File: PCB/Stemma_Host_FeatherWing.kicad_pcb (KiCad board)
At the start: 2 copper layers, 50.8 x 22.9 mm, 17 parts, among them J1 STEMMA, J2 STEMMA, J3 STEMMA-QT, J4 STEMMA-QT, M1 Feather_M4_Express, U1 BSS138DW-Y-F_ALT, U2 AP2112-3.3

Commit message: update with initial design
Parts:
- removed C2: 0.1uF, Capacitors_SMD:C_0805
- removed C3: 10uF, Capacitors_SMD:C_0805
- removed U2: AP2112-3.3, TO_SOT_Packages_SMD:SOT-23-5
- added D2: MBR120, Diodes_SMD:D_SOD-123F, F.Cu at (122.1, 99.8)
- added D3: MBR120, Diodes_SMD:D_SOD-123F, F.Cu at (125.7, 99.8)
- added SW1: RESET, Adafruit:TL3330AF_SPST_BUTTON_RT-ANGLE_7.8mm_2.5mm_2.5mm, F.Cu at (117.3, 85.5)
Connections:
- M1 pad 1: (no net) -> /~RST
- M1 pad 17: (no net) -> /BAT
- M1 pad 19: (no net) -> /USB
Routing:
- net /USB: track 0.00 -> 31.2 mm, vias 0 -> 1
- net /~RST: track 0.00 -> 24.0 mm, vias 0 -> 1
- net /BAT: track 0.00 -> 22.7 mm, vias 0 -> 1
- net /+V: track 84.3 -> 72.1 mm, vias 4 -> 3
- net +3V3: track 39.4 -> 35.4 mm
- net GND: vias 13 -> 14
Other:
- board text added: "2019-11-26 v01"
- board text added: "A Feather-powered Stemma FeatherWing. The host Feather provides 3.3V or ~5V for the Stemma connector."
- board text added: "Stemma Host FeatherWing"
- board text removed: "2019-11-26 v02"
- board text removed: "A Stemma-powered interface backpack for FeatherWings. The Stemma connector provides +3.3V to the attached Wing."
- board text removed: "StemmaWing Backpack"

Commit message: update design
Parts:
- added JMP3: STEMMA_TYPE, Connectors:GS3, B.Cu at (141.7, 109.5)
- SW1: value RESET -> SW_Push
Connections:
- J1 pad 3: /+V -> Net-(J1-Pad3)
- J2 pad 3: /+V -> Net-(J1-Pad3)
- J3 pad 3: /+V -> Net-(J1-Pad3)
- J4 pad 3: /+V -> Net-(J1-Pad3)
- RN1 pad 1: /+V -> Net-(J1-Pad3)
- RN1 pad 4: /+V -> Net-(J1-Pad3)
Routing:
- net /+V: track 72.1 -> 74.1 mm
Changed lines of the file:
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@@
     (thickness 1.6)
     (drawings 3434)
-    (tracks 255)
+    (tracks 257)
     (zones 0)
-    (modules 17)
-    (nets 14)
+    (modules 18)
+    (nets 15)
   )
   (page USLetter)
@@
     (35 F.Paste user hide)
     (36 B.SilkS user)
-    (37 F.SilkS user)
+    (37 F.SilkS user hide)
     (38 B.Mask user)
-    (39 F.Mask user)
+    (39 F.Mask user hide)
     (40 Dwgs.User user hide)
     (41 Cmts.User user hide)
@@
   (net 12 /USB)
   (net 13 /~RST)
+  (net 14 "Net-(J1-Pad3)")
   (net_class Default "This is the default net class."
     (clearance 0.1524)
@@
     (add_net /~RST)
     (add_net "Net-(D1-Pad2)")
+    (add_net "Net-(J1-Pad3)")
   )
   (net_class Power ""
@@
       (net 1 GND))
     (pad 3 smd rect (at 0.5 -1.9375 270) (size 0.6 1.55) (layers F.Cu F.Paste F.Mask)
-      (net 7 /+V))
+      (net 14 "Net-(J1-Pad3)"))
     (pad 2 smd rect (at -0.5 -1.9375 270) (size 0.6 1.55) (layers F.Cu F.Paste F.Mask)
       (net 6 /STEMMA_SDA))
@@
       (net 1 GND))
     (pad 3 smd rect (at 0.5 -1.9375 90) (size 0.6 1.55) (layers F.Cu F.Paste F.Mask)
-      (net 7 /+V))
+      (net 14 "Net-(J1-Pad3)"))
     (pad 2 smd rect (at -0.5 -1.9375 90) (size 0.6 1.55) (layers F.Cu F.Paste F.Mask)
       (net 6 /STEMMA_SDA))
@@
       (net 3 /SDA))
     (pad 4 smd rect (at -0.9 1.2) (size 0.8 0.5) (layers F.Cu F.Paste F.Mask)
-      (net 7 /+V))
+      (net 14 "Net-(J1-Pad3)"))
     (pad 2 smd rect (at -0.9 -0.4) (size 0.8 0.4) (layers F.Cu F.Paste F.Mask)
       (net 4 +3V3))
@@
       (net 4 +3V3))
     (pad 1 smd rect (at -0.9 -1.2) (size 0.8 0.5) (layers F.Cu F.Paste F.Mask)
-      (net 7 /+V))
+      (net 14 "Net-(J1-Pad3)"))
     (model ${KISYS3DMOD}/Resistors_SMD.3dshapes/R_Array_Convex_4x0603.wrl
       (at (xyz 0 0 0))
@@
       (net 6 /STEMMA_SDA))
     (pad 3 smd rect (at 1 -2.875 270) (size 1 3.5) (layers F.Cu F.Paste F.Mask)
-      (net 7 /+V))
+      (net 14 "Net-(J1-Pad3)"))
     (pad 4 smd rect (at 3 -2.875 270) (size 1 3.5) (layers F.Cu F.Paste F.Mask)
       (net 1 GND))
@@
       (net 1 GND))
     (pad 3 smd rect (at 1 -2.875 90) (size 1 3.5) (layers F.Cu F.Paste F.Mask)
-      (net 7 /+V))
+      (net 14 "Net-(J1-Pad3)"))
     (pad 2 smd rect (at -1 -2.875 90) (size 1 3.5) (layers F.Cu F.Paste F.Mask)
       (net 6 /STEMMA_SDA))
@@
       (effects (font (size 0.5 0.5) (thickness 0.1)))
     )
-    (fp_text value RESET (at 0 2.1) (layer F.SilkS)
+    (fp_text value SW_Push (at 0 2.1) (layer F.SilkS)
       (effects (font (size 0.6 0.6) (thickness 0.12)))
     )
@@
     )
   )
+  (module Connectors:GS3 (layer B.Cu)
+    (at 141.7 109.5)
+    (descr "3-pin solder bridge")
+    (tags "solder bridge")
+    (attr smd)
+    (fp_text reference JMP3 (at -1.7 0 -90) (layer B.SilkS)
+      (effects (font (size 1 1) (thickness 0.15)) (justify mirror))
+    )
+    (fp_text value STEMMA_TYPE (at 1.8 0 -90) (layer B.Fab)
+      (effects (font (size 1 1) (thickness 0.15)) (justify mirror))
+    )
+    (fp_line (start -1.15 2.15) (end 1.15 2.15) (layer B.CrtYd) (width 0.05))
+    (fp_line (start 1.15 2.15) (end 1.15 -2.15) (layer B.CrtYd) (width 0.05))
+    (fp_line (start 1.15 -2.15) (end -1.15 -2.15) (layer B.CrtYd) (width 0.05))
+    (fp_line (start -1.15 -2.15) (end -1.15 2.15) (layer B.CrtYd) (width 0.05))
+    (fp_line (start -0.89 1.91) (end -0.89 -1.91) (layer B.SilkS) (width 0.12))
+    (fp_line (start -0.89 -1.91) (end 0.89 -1.91) (layer B.SilkS) (width 0.12))
+    (fp_line (start 0.89 -1.91) (end 0.89 1.91) (layer B.SilkS) (width 0.12))
+    (fp_line (start -0.89 1.91) (end 0.89 1.91) (layer B.SilkS) (width 0.12))
+    (pad 1 smd rect (at 0 1.27) (size 1.27 0.97) (layers B.Cu B.Paste B.Mask)
+      (net 4 +3V3))
+    (pad 2 smd rect (at 0 0) (size 1.27 0.97) (layers B.Cu B.Paste B.Mask)
+      (net 14 "Net-(J1-Pad3)"))
+    (pad 3 smd rect (at 0 -1.27) (size 1.27 0.97) (layers B.Cu B.Paste B.Mask)
+      (net 7 /+V))
+  )
   (gr_line (start 144.970789 88.408715) (end 144.970789 88.387715) (layer F.SilkS) (width 0.1))
   (gr_line (start 145.055489 88.324715) (end 145.055489 88.302715) (layer F.SilkS) (width 0.1))
@@
   (segment (start 129.421937 101.2) (end 129.880683 101.658746) (width 0.1524) (layer F.Cu) (net 7))
   (segment (start 125.7 101.2) (end 129.421937 101.2) (width 0.1524) (layer F.Cu) (net 7))
+  (segment (start 155.829 94.75) (end 155.829 93.129) (width 0.1524) (layer B.Cu) (net 7))
+  (segment (start 155.829 93.129) (end 155.5 92.8) (width 0.1524) (layer B.Cu) (net 7))
   (segment (start 132.969 99.908746) (end 132.969 99.406346) (width 0.1524) (layer F.Cu) (net 8))
   (segment (start 132.969 99.406346) (end 132.969 98.171) (width 0.1524) (layer F.Cu) (net 8))

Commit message: initial repo load
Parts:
- SW1: value SW_Push -> RESET
- U1: value BSS138DW-Y-F_ALT -> BSS138DW-Y-F
- moved JMP3 33.5 mm to (113.9, 90.8)
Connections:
- J1 pad 3: Net-(J1-Pad3) -> /+V
- J2 pad 3: Net-(J1-Pad3) -> /+V
- J3 pad 3: Net-(J1-Pad3) -> /+V
- J4 pad 3: Net-(J1-Pad3) -> /+V
- JMP3 pad 2: Net-(J1-Pad3) -> /+V
- RN1 pad 1: Net-(J1-Pad3) -> /+V
- RN1 pad 4: Net-(J1-Pad3) -> /+V
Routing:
- net /+V: track 74.1 -> 120.9 mm, vias 3 -> 4
- net +3V3: track 35.4 -> 52.5 mm, vias 0 -> 1
- net /STEMMA_SDA: track 48.0 -> 53.6 mm
- net /STEMMA_SCL: track 51.6 -> 49.5 mm
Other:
- board text added: "2019-11-27 v01"
- board text added: "3V"
- board text added: "A Feather-powered Stemma FeatherWing. The host Feather provides 3.3V or ~~5V for the Stemma connector."
- board text added: "Stemma +V"
- board text added: "~~5V"
- board text removed: "2019-11-26 v01"
- board text removed: "A Feather-powered Stemma FeatherWing. The host Feather provides 3.3V or ~5V for the Stemma connector."

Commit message: PCB version update
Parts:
- U1: value BSS138DW-Y-F -> BSS138; footprint TO_SOT_Packages_SMD:SOT-23-6 -> TO_SOT_Packages_SMD:SOT-363_SC-70-6
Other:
- board text added: "2019-12-09 v02"
- board text removed: "2019-11-27 v01"

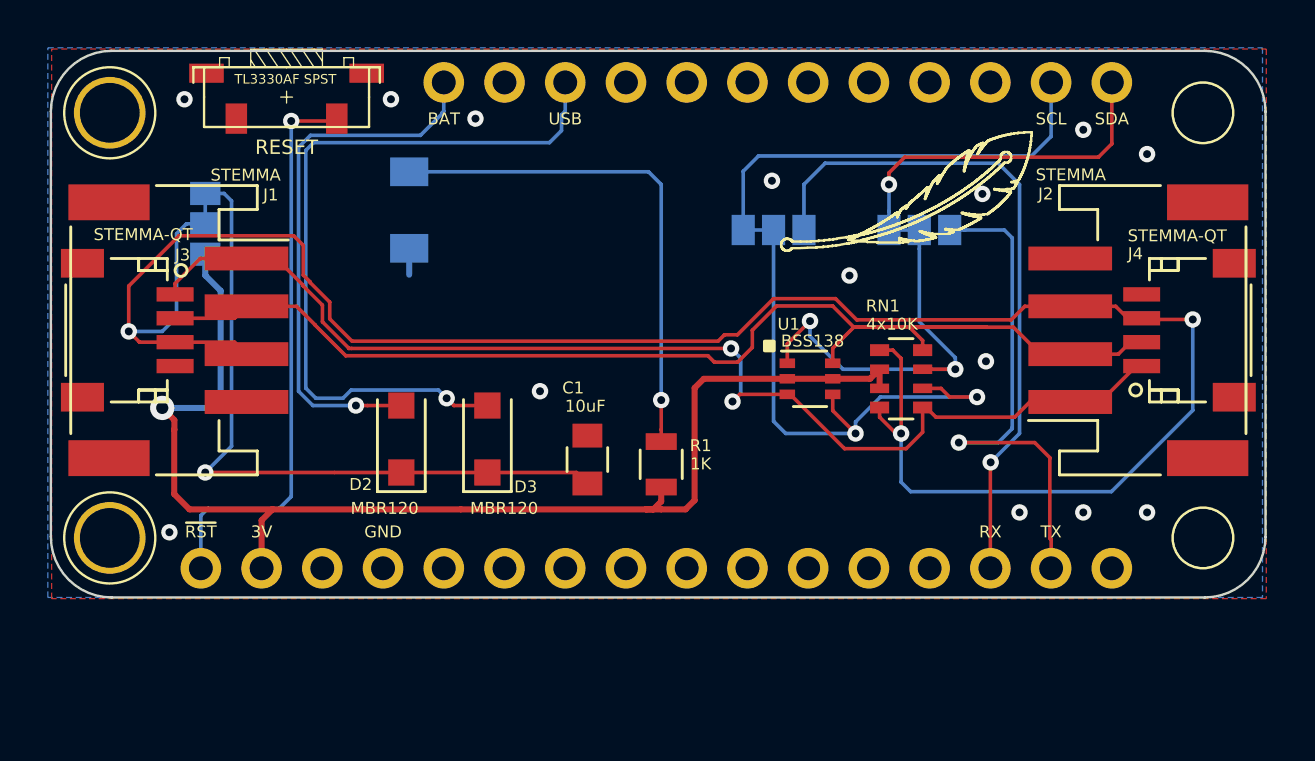
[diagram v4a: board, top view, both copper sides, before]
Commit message: correct stemma-qt pinout
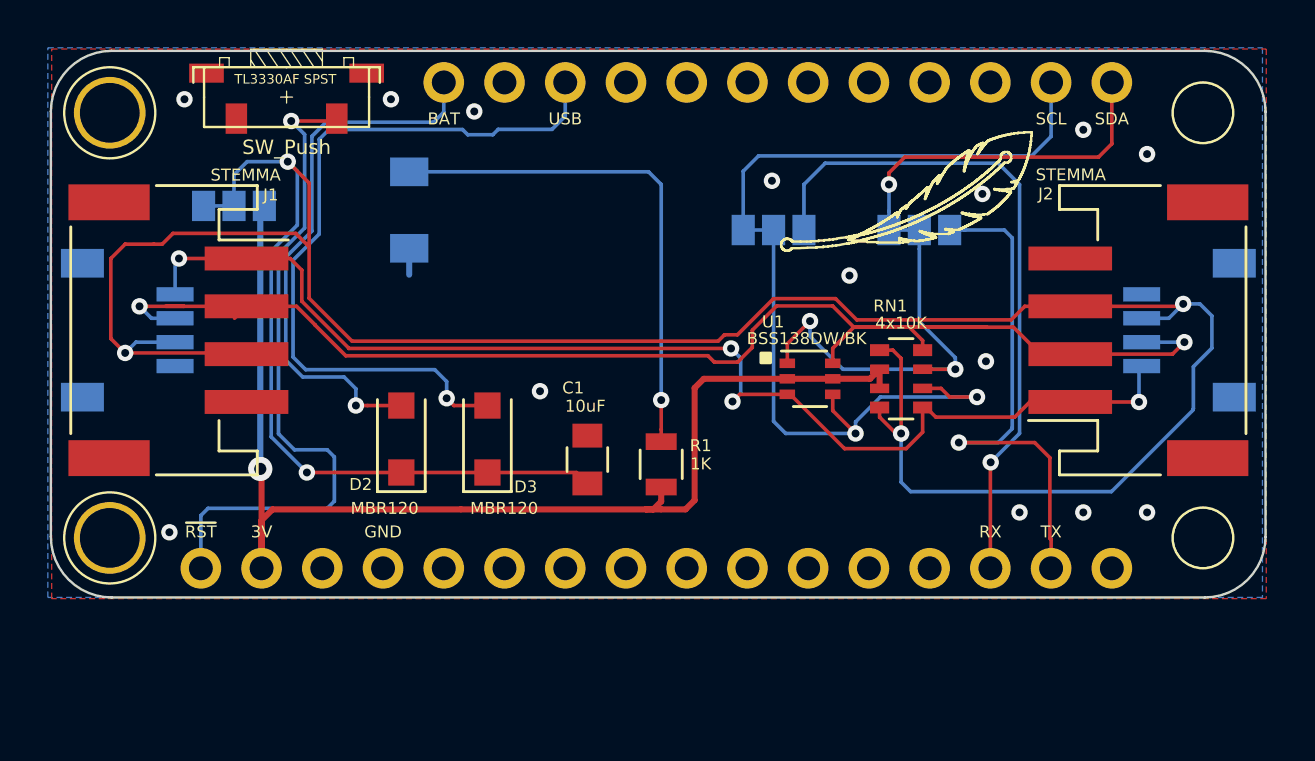
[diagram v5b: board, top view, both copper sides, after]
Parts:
- added G***: LOGO, Adafruit:CG_logo_25-4mm, B.Cu at (113.8, 96.2)
- J3, J4: moved to B.Cu
- SW1: value RESET -> SW_Push
- U1: value BSS138 -> BSS138DW/BK
- moved G*** 17.3 mm to (130.2, 93.2)
- moved G*** 11.6 mm to (131.0, 89.0)
- moved JMP3 1.42 mm to (115.1, 90.0), turned to 90 degrees
- turned J3 to 90 degrees
- turned J4 to 270 degrees
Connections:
- J3 pad 1: /STEMMA_SCL -> GND
- J3 pad 2: /STEMMA_SDA -> /+V
- J3 pad 3: /+V -> /STEMMA_SDA
- J3 pad 4: GND -> /STEMMA_SCL
- J4 pad 1: /STEMMA_SCL -> GND
- J4 pad 2: /STEMMA_SDA -> /+V
- J4 pad 3: /+V -> /STEMMA_SDA
- J4 pad 4: GND -> /STEMMA_SCL
- M1 pad 10: (no net) -> /A5
- M1 pad 11: (no net) -> /SCK
- M1 pad 12: (no net) -> /MO
- M1 pad 13: (no net) -> /MI
- M1 pad 16: (no net) -> /D4
- M1 pad 18: (no net) -> /EN
- M1 pad 20: (no net) -> /D13-LED
- M1 pad 21: (no net) -> /D12
- M1 pad 22: (no net) -> /D11
- M1 pad 23: (no net) -> /D10
- M1 pad 24: (no net) -> /D9
- M1 pad 25: (no net) -> /D6
- M1 pad 26: (no net) -> /D5
- M1 pad 3: (no net) -> /Aref
- M1 pad 5: (no net) -> /~~A0
- M1 pad 6: (no net) -> /~~A1
- M1 pad 7: (no net) -> /A2
- M1 pad 8: (no net) -> /A3
- M1 pad 9: (no net) -> /A4
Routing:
- net /STEMMA_SDA: track 53.9 -> 61.9 mm, vias 0 -> 2
- net /+V: track 120.9 -> 126.7 mm, vias 4 -> 5
- net /~RST: track 24.0 -> 28.3 mm
- net /STEMMA_SCL: track 49.5 -> 52.4 mm, vias 2 -> 4
- net +3V3: track 52.5 -> 50.7 mm
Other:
- board text added: "20120-07-31 v03"
- board text added: "A Feather-powered Stemma FeatherWing. The host Feather provides 3.3V or ~~5V for the Stemma connectors."
- board text added: "HOST"
- board text removed: "2019-12-09 v02"
- board text removed: "A Feather-powered Stemma FeatherWing. The host Feather provides 3.3V or ~~5V for the Stemma connector."
